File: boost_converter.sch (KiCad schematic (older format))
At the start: 20 parts, among them SW1 SW_Push, U1 LTC2955-1(DFN), U2 LTC3458

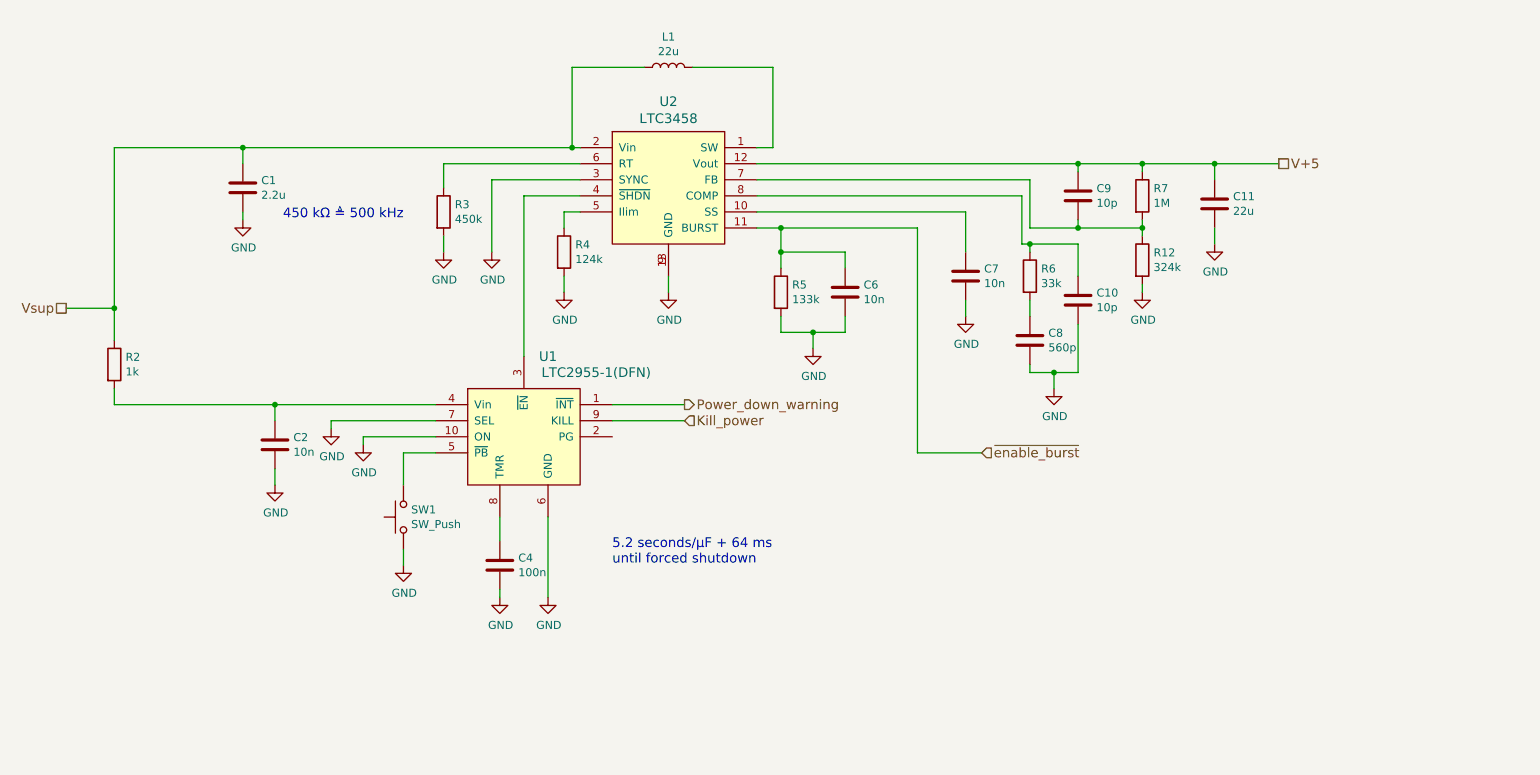
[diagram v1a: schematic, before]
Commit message: Moved MCU pins around to make sure that they do not interfere with the programmer Moved ISP Header closer to the edge of the board to allow easier access with the programmer Added pulldown resistor to the DCD/DC converters enable pin to make sure it stays off in case of failure Added more PDFs of components
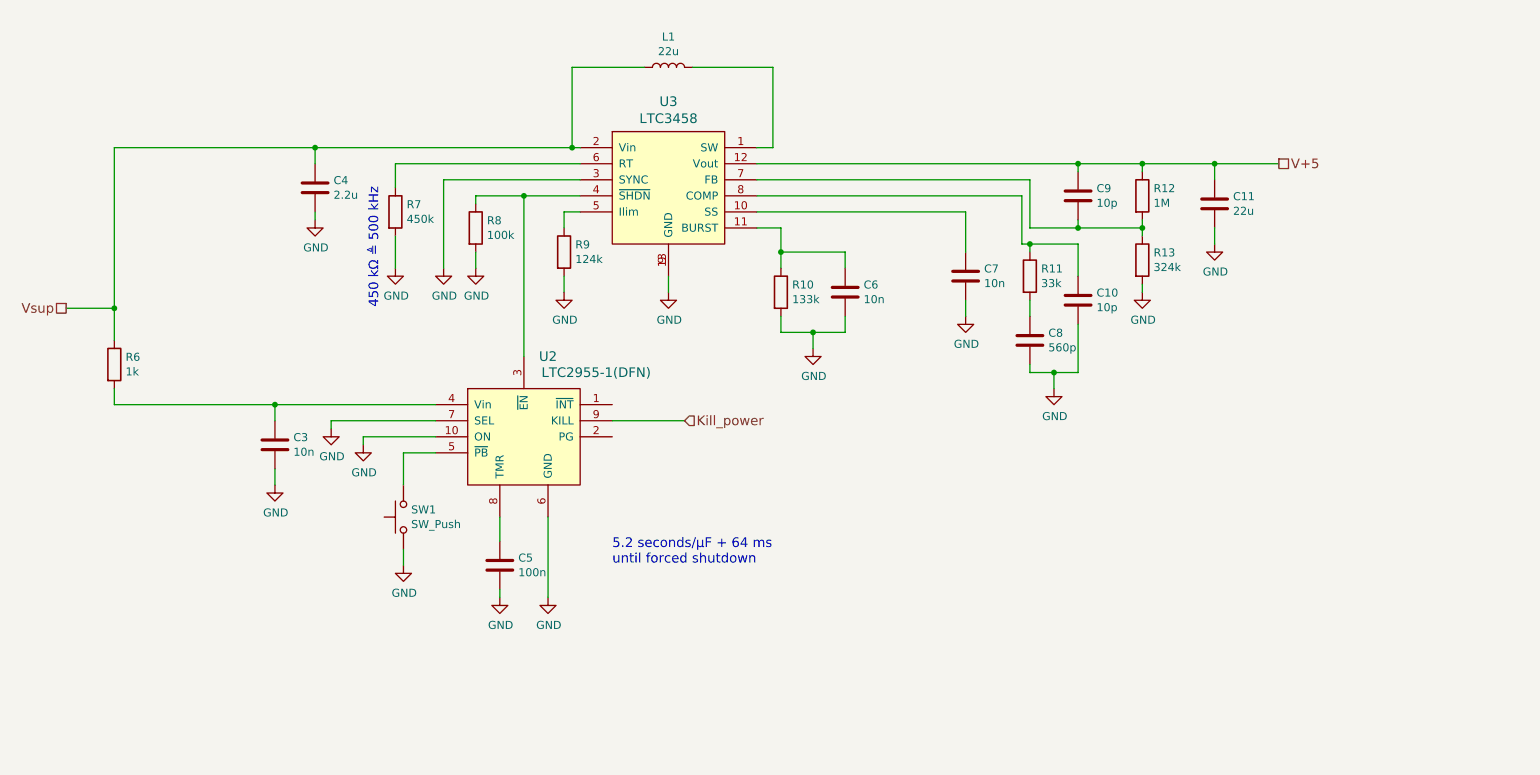
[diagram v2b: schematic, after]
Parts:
- added R8: 100k, Resistors_SMD:R_0603, symbol R
- renumbered C2 to C3, C1 to C4, C4 to C5, R5 to R10, R6 to R11, R7 to R12, R12 to R13, R2 to R6, R3 to R7, R4 to R9, U1 to U2, U2 to U3
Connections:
- net GND: now also R8.2
- net at U2.3 (~EN), U3.4 (~SHDN): now also R8.1
- net Power_down_warning: no longer names the net of U2.1 (~INT)
- net ~enable_burst: no longer names the net of C6.1, R10.1, U3.11 (BURST)
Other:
- moved on the sheet: C4, R7
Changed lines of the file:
@@
 $EndDescr
 $Comp
-L LTC2955-1(DFN) U1
+L LTC2955-1(DFN) U2
 U 1 1 59D06F4F
 P 4850 3600
-F 0 "U1" H 5000 4250 60  0000 C CNN
+F 0 "U2" H 5000 4250 60  0000 C CNN
 F 1 "LTC2955-1(DFN)" H 5300 4150 60  0000 C CNN
 F 2 "Housings_DFN_QFN:DFN-10-1EP_2x3mm_Pitch0.5mm" H 6200 4250 60  0001 C CNN
@@
 Vsup
 $Comp
-L C C2
+L C C3
 U 1 1 59D07029
 P 3300 3500
-F 0 "C2" H 3415 3546 50  0000 L CNN
+F 0 "C3" H 3415 3546 50  0000 L CNN
 F 1 "10n" H 3415 3455 50  0000 L CNN
 F 2 "Capacitors_SMD:C_0603" H 3338 3350 50  0001 C CNN
@@
 $EndComp
 $Comp
-L C C4
+L C C5
 U 1 1 59D073A5
 P 4700 4250
-F 0 "C4" H 4815 4296 50  0000 L CNN
+F 0 "C5" H 4815 4296 50  0000 L CNN
 F 1 "100n" H 4815 4205 50  0000 L CNN
 F 2 "Capacitors_SMD:C_0603" H 4738 4100 50  0001 C CNN
@@
 $EndComp
 $Comp
-L R R2
+L R R6
 U 1 1 59D07A41
 P 2300 3000
-F 0 "R2" H 2370 3046 50  0000 L CNN
+F 0 "R6" H 2370 3046 50  0000 L CNN
 F 1 "1k" H 2370 2955 50  0000 L CNN
 F 2 "Resistors_SMD:R_0603" V 2230 3000 50  0001 C CNN
@@
 $EndComp
 $Comp
-L LTC3458 U2
+L LTC3458 U3
 U 1 1 59D08D68
 P 5750 2000
-AR Path="/59D08D68" Ref="U2"  Part="1"
-AR Path="/59B6A868/59D05F37/59D08D68" Ref="U2"  Part="1"
-F 0 "U2" H 5750 2637 60  0000 C CNN
+F 0 "U3" H 5750 2637 60  0000 C CNN
 F 1 "LTC3458" H 5750 2531 60  0000 C CNN
 F 2 "Housings_DFN_QFN:DFN-12-1EP_3x4mm_Pitch0.5mm" H 7100 2650 60  0001 C CNN
@@
 $EndComp
 $Comp
-L R R3
+L R R7
 U 1 1 59D08F18
-P 4350 2050
-F 0 "R3" H 4420 2096 50  0000 L CNN
-F 1 "450k" H 4420 2005 50  0000 L CNN
-F 2 "Resistors_SMD:R_0603" V 4280 2050 50  0001 C CNN
-F 3 "" H 4350 2050 50  0001 C CNN
-	1    4350 2050
+P 4050 2050
+F 0 "R7" H 4120 2096 50  0000 L CNN
+F 1 "450k" H 4120 2005 50  0000 L CNN
+F 2 "Resistors_SMD:R_0603" V 3980 2050 50  0001 C CNN
+F 3 "" H 4050 2050 50  0001 C CNN
+	1    4050 2050
 	1    0    0    -1
 $EndComp
@@
 L GND #PWR017
 U 1 1 59D08FA8
-P 4350 2300
-F 0 "#PWR017" H 4350 2050 50  0001 C CNN
-F 1 "GND" H 4355 2127 50  0000 C CNN
-F 2 "" H 4350 2300 50  0001 C CNN
-F 3 "" H 4350 2300 50  0001 C CNN
-	1    4350 2300
-	1    0    0    -1
-$EndComp
-Text Notes 3350 2100 0    60   ~ 0
+P 4050 2400
+F 0 "#PWR017" H 4050 2150 50  0001 C CNN
+F 1 "GND" H 4055 2227 50  0000 C CNN
+F 2 "" H 4050 2400 50  0001 C CNN
+F 3 "" H 4050 2400 50  0001 C CNN
+	1    4050 2400
+	1    0    0    -1
+$EndComp
+Text Notes 3950 2650 1    60   ~ 0
 450 kΩ ≜ 500 kHz
 $Comp
 L GND #PWR018
 U 1 1 59D09261
-P 4650 2300
-F 0 "#PWR018" H 4650 2050 50  0001 C CNN
-F 1 "GND" H 4655 2127 50  0000 C CNN
-F 2 "" H 4650 2300 50  0001 C CNN
-F 3 "" H 4650 2300 50  0001 C CNN
-	1    4650 2300
-	1    0    0    -1
-$EndComp
-$Comp
-L R R4
+P 4350 2400
+F 0 "#PWR018" H 4350 2150 50  0001 C CNN
+F 1 "GND" H 4355 2227 50  0000 C CNN
+F 2 "" H 4350 2400 50  0001 C CNN
+F 3 "" H 4350 2400 50  0001 C CNN
+	1    4350 2400
+	1    0    0    -1
+$EndComp
+$Comp
+L R R9
 U 1 1 59D092D3
 P 5100 2300
-F 0 "R4" H 5170 2346 50  0000 L CNN
+F 0 "R9" H 5170 2346 50  0000 L CNN
 F 1 "124k" H 5170 2255 50  0000 L CNN
 F 2 "Resistors_SMD:R_0603" V 5030 2300 50  0001 C CNN
@@
 $EndComp
 $Comp
-L R R7
+L R R12
 U 1 1 59D096F1
 P 8700 1950
-F 0 "R7" H 8770 1996 50  0000 L CNN
+F 0 "R12" H 8770 1996 50  0000 L CNN
 F 1 "1M" H 8770 1905 50  0000 L CNN
 F 2 "Resistors_SMD:R_0603" V 8630 1950 50  0001 C CNN
@@
 $EndComp
 $Comp
-L R R12
+L R R13
 U 1 1 59D09733
 P 8700 2350
-F 0 "R12" H 8770 2396 50  0000 L CNN
+F 0 "R13" H 8770 2396 50  0000 L CNN
 F 1 "324k" H 8770 2305 50  0000 L CNN
 F 2 "Resistors_SMD:R_0603" V 8630 2350 50  0001 C CNN
@@
 $EndComp
 $Comp
-L R R6
+L R R11
 U 1 1 59D09D45
 P 8000 2450
-F 0 "R6" H 8070 2496 50  0000 L CNN
+F 0 "R11" H 8070 2496 50  0000 L CNN
 F 1 "33k" H 8070 2405 50  0000 L CNN
 F 2 "Resistors_SMD:R_0603" V 7930 2450 50  0001 C CNN
@@
 $EndComp
 $Comp
-L R R5
+L R R10
 U 1 1 59D0A192
 P 6450 2550
-F 0 "R5" H 6520 2596 50  0000 L CNN
+F 0 "R10" H 6520 2596 50  0000 L CNN
 F 1 "133k" H 6520 2505 50  0000 L CNN
 F 2 "Resistors_SMD:R_0603" V 6380 2550 50  0001 C CNN
@@
 	6450 2150 6450 2400
 Wire Wire Line
-	6300 2150 7300 2150
-Wire Wire Line
 	7600 2600 7600 2700
 Wire Wire Line
@@
 	5100 2550 5100 2450
 Wire Wire Line
-	4650 1850 4650 2300
-Wire Wire Line
-	5200 1850 4650 1850
-Wire Wire Line
-	4350 2300 4350 2200
-Wire Wire Line
-	4350 1750 4350 1900
-Wire Wire Line
-	5200 1750 4350 1750
-Wire Wire Line
-	4850 1950 5200 1950
+	4350 1850 4350 2400
+Wire Wire Line
+	5200 1850 4350 1850
+Wire Wire Line
+	4050 2400 4050 2200
+Wire Wire Line
+	4050 1750 4050 1900
+Wire Wire Line
+	5200 1750 4050 1750
+Wire Wire Line
+	4550 1950 5200 1950
 Wire Wire Line
 	4850 2950 4850 1950
@@
 Connection ~ 5150 1650
 $Comp
-L C C1
+L C C4
 U 1 1 59D0AC39
-P 3100 1900
-F 0 "C1" H 3215 1946 50  0000 L CNN
-F 1 "2.2u" H 3215 1855 50  0000 L CNN
-F 2 "Capacitors_SMD:C_0603" H 3138 1750 50  0001 C CNN
-F 3 "" H 3100 1900 50  0001 C CNN
-	1    3100 1900
+P 3550 1900
+F 0 "C4" H 3665 1946 50  0000 L CNN
+F 1 "2.2u" H 3665 1855 50  0000 L CNN
+F 2 "Capacitors_SMD:C_0603" H 3588 1750 50  0001 C CNN
+F 3 "" H 3550 1900 50  0001 C CNN
+	1    3550 1900
 	1    0    0    -1
 $EndComp
@@
 L GND #PWR025
 U 1 1 59D0AC9B
-P 3100 2100
-F 0 "#PWR025" H 3100 1850 50  0001 C CNN
-F 1 "GND" H 3105 1927 50  0000 C CNN
-F 2 "" H 3100 2100 50  0001 C CNN
-F 3 "" H 3100 2100 50  0001 C CNN
-	1    3100 2100
-	1    0    0    -1
-$EndComp
-Wire Wire Line
-	3100 2100 3100 2050
-Wire Wire Line
-	3100 1750 3100 1650
-Connection ~ 3100 1650
+P 3550 2100
+F 0 "#PWR025" H 3550 1850 50  0001 C CNN
+F 1 "GND" H 3555 1927 50  0000 C CNN
+F 2 "" H 3550 2100 50  0001 C CNN
+F 3 "" H 3550 2100 50  0001 C CNN
+	1    3550 2100
+	1    0    0    -1
+$EndComp
+Wire Wire Line
+	3550 2100 3550 2050
+Wire Wire Line
+	3550 1750 3550 1650
+Connection ~ 3550 1650
 $Comp
 L C C11
@@
 	9150 1850 9150 1750
 Connection ~ 9150 1750
-Text HLabel 5850 3250 2    60   Output ~ 0
-Power_down_warning
-Wire Wire Line
-	5400 3250 5850 3250
 Text HLabel 5850 3350 2    60   Input ~ 0
 Kill_power
 Wire Wire Line
 	5850 3350 5400 3350
-Text HLabel 7700 3550 2    60   Input ~ 0
-~enable_burst
-Wire Wire Line
-	7300 2150 7300 3550
-Wire Wire Line
-	7300 3550 7700 3550
-Connection ~ 6450 2150
+Wire Wire Line
+	6300 2150 6450 2150
+$Comp
+L GND #PWR027
+U 1 1 5A46F400
+P 4550 2400
+F 0 "#PWR027" H 4550 2150 50  0001 C CNN
+F 1 "GND" H 4555 2227 50  0000 C CNN
+F 2 "" H 4550 2400 50  0001 C CNN
+F 3 "" H 4550 2400 50  0001 C CNN
+	1    4550 2400
+	1    0    0    -1
+$EndComp
+Wire Wire Line
+	4550 2000 4550 1950
+Connection ~ 4850 1950
+Wire Wire Line
+	4550 2300 4550 2400
+$Comp
+L R R8
+U 1 1 5A46F9EB
+P 4550 2150
+F 0 "R8" H 4620 2196 50  0000 L CNN
+F 1 "100k" H 4620 2105 50  0000 L CNN
+F 2 "Resistors_SMD:R_0603" H 4620 2059 50  0001 L CNN
+F 3 "" H 4550 2150 50  0000 C CNN
+	1    4550 2150
+	1    0    0    -1
+$EndComp
 $EndSCHEMATC

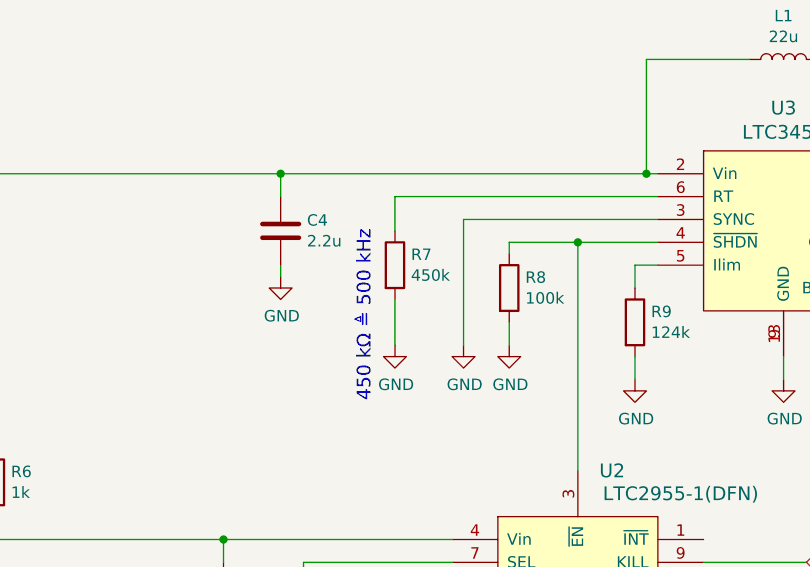
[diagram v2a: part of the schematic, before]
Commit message: Added part names and BOM Added Gerber files
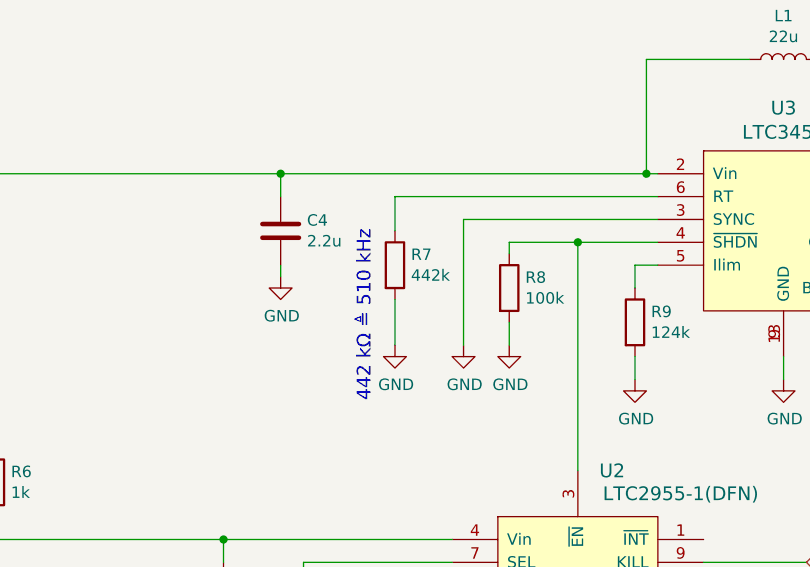
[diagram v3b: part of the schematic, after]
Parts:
- C10, C9: MFN (none) -> Murata; MFP (none) -> GCM1885C1H100FA16D
- C11: MFN (none) -> Murata; MFP (none) -> GRM31CR61E226KE15K
- C3, C6, C7: MFN (none) -> Murata; MFP (none) -> GRM1885C1H103JA01D
- C4: MFN (none) -> Murata; MFP (none) -> GRM188R61E225KA12D
- C5: MFN (none) -> Murata; MFP (none) -> GRM188R71H104KA93D
- C8: MFN (none) -> Murata; MFP (none) -> GCM1885C2A561JA16D
- R10: MFN (none) -> Susumu; MFP (none) -> RR0816P-1333-D-13D
- R11: MFN (none) -> Susumu; MFP (none) -> RR0816P-333-D
- R12: MFN (none) -> Yageo; MFP (none) -> RC0603FR-101ML
- R13: MFN (none) -> Susumu; MFP (none) -> RR0816P-3243-D-50D
- R6: MFN (none) -> Yageo; MFP (none) -> RC0603FR-071KL
- R7: value 450k -> 442k; MFN (none) -> Yageo; MFP (none) -> RT0603DRE07442KL
- R8: MFN (none) -> Yageo; MFP (none) -> RC0603JR-07100KL
- R9: MFN (none) -> Susumu; MFP (none) -> RR0816P-1243-D-10D
- SW1: footprint SW_Tactile_SPST_Angled_PTS645Vx31-2LFS -> Buttons_Switches_THT:SW_Tactile_SPST_Angled_PTS645Vx31-2LFS; MFN (none) -> C&K Components; MFP (none) -> PTS645VL31-2 LFS
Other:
- note added: "442 kΩ ≜ 510 kHz"
- note removed: "450 kΩ ≜ 500 kHz"
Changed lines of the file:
@@
 F 2 "Capacitors_SMD:C_0603" H 3338 3350 50  0001 C CNN
 F 3 "" H 3300 3500 50  0001 C CNN
+F 4 "Murata" H 3300 3500 60  0001 C CNN "MFN"
+F 5 "GRM1885C1H103JA01D" H 3300 3500 60  0001 C CNN "MFP"
 	1    3300 3500
 	1    0    0    -1
@@
 F 0 "SW1" V 4146 3902 50  0000 R CNN
 F 1 "SW_Push" V 4055 3902 50  0000 R CNN
-F 2 "SW_Tactile_SPST_Angled_PTS645Vx31-2LFS" H 4100 4150 50  0001 C CNN
+F 2 "Buttons_Switches_THT:SW_Tactile_SPST_Angled_PTS645Vx31-2LFS" H 4100 4150 50  0001 C CNN
 F 3 "" H 4100 4150 50  0001 C CNN
+F 4 "C&K Components" H 4100 3950 60  0001 C CNN "MFN"
+F 5 "PTS645VL31-2 LFS" H 4100 3950 60  0001 C CNN "MFP"
 	1    4100 3950
 	0    -1   -1   0
@@
 F 2 "Capacitors_SMD:C_0603" H 4738 4100 50  0001 C CNN
 F 3 "" H 4700 4250 50  0001 C CNN
+F 4 "Murata" H 4700 4250 60  0001 C CNN "MFN"
+F 5 "GRM188R71H104KA93D" H 4700 4250 60  0001 C CNN "MFP"
 	1    4700 4250
 	1    0    0    -1
@@
 F 2 "Resistors_SMD:R_0603" V 2230 3000 50  0001 C CNN
 F 3 "" H 2300 3000 50  0001 C CNN
+F 4 "Yageo" H 2300 3000 60  0001 C CNN "MFN"
+F 5 "RC0603FR-071KL" H 2300 3000 60  0001 C CNN "MFP"
 	1    2300 3000
 	1    0    0    -1
@@
 P 4050 2050
 F 0 "R7" H 4120 2096 50  0000 L CNN
-F 1 "450k" H 4120 2005 50  0000 L CNN
+F 1 "442k" H 4120 2005 50  0000 L CNN
 F 2 "Resistors_SMD:R_0603" V 3980 2050 50  0001 C CNN
 F 3 "" H 4050 2050 50  0001 C CNN
+F 4 "Yageo" H 4050 2050 60  0001 C CNN "MFN"
+F 5 "RT0603DRE07442KL" H 4050 2050 60  0001 C CNN "MFP"
 	1    4050 2050
 	1    0    0    -1
@@
 $EndComp
 Text Notes 3950 2650 1    60   ~ 0
-450 kΩ ≜ 500 kHz
+442 kΩ ≜ 510 kHz
 $Comp
 L GND #PWR018
@@
 F 2 "Resistors_SMD:R_0603" V 5030 2300 50  0001 C CNN
 F 3 "" H 5100 2300 50  0001 C CNN
+F 4 "Susumu" H 5100 2300 60  0001 C CNN "MFN"
+F 5 "RR0816P-1243-D-10D" H 5100 2300 60  0001 C CNN "MFP"
 	1    5100 2300
 	1    0    0    -1
@@
 F 2 "Capacitors_SMD:C_0603" H 8338 1800 50  0001 C CNN
 F 3 "" H 8300 1950 50  0001 C CNN
+F 4 "Murata" H 8300 1950 60  0001 C CNN "MFN"
+F 5 "GCM1885C1H100FA16D" H 8300 1950 60  0001 C CNN "MFP"
 	1    8300 1950
 	1    0    0    -1
@@
 F 2 "Resistors_SMD:R_0603" V 8630 1950 50  0001 C CNN
 F 3 "" H 8700 1950 50  0001 C CNN
+F 4 "Yageo" H 8700 1950 60  0001 C CNN "MFN"
+F 5 "RC0603FR-101ML" H 8700 1950 60  0001 C CNN "MFP"
 	1    8700 1950
 	1    0    0    -1
@@
 F 2 "Resistors_SMD:R_0603" V 8630 2350 50  0001 C CNN
 F 3 "" H 8700 2350 50  0001 C CNN
+F 4 "Susumu" H 8700 2350 60  0001 C CNN "MFN"
+F 5 "RR0816P-3243-D-50D" H 8700 2350 60  0001 C CNN "MFP"
 	1    8700 2350
 	1    0    0    -1
@@
 F 2 "Capacitors_SMD:C_0603" H 8038 2700 50  0001 C CNN
 F 3 "" H 8000 2850 50  0001 C CNN
+F 4 "Murata" H 8000 2850 60  0001 C CNN "MFN"
+F 5 "GCM1885C2A561JA16D" H 8000 2850 60  0001 C CNN "MFP"
 	1    8000 2850
 	1    0    0    -1
@@
 F 2 "Capacitors_SMD:C_0603" H 8338 2450 50  0001 C CNN
 F 3 "" H 8300 2600 50  0001 C CNN
+F 4 "Murata" H 8300 2600 60  0001 C CNN "MFN"
+F 5 "GCM1885C1H100FA16D" H 8300 2600 60  0001 C CNN "MFP"
 	1    8300 2600
 	1    0    0    -1
@@
 F 2 "Resistors_SMD:R_0603" V 7930 2450 50  0001 C CNN
 F 3 "" H 8000 2450 50  0001 C CNN
+F 4 "Susumu" H 8000 2450 60  0001 C CNN "MFN"
+F 5 "RR0816P-333-D" H 8000 2450 60  0001 C CNN "MFP"
 	1    8000 2450
 	1    0    0    -1
@@
 F 2 "Capacitors_SMD:C_0603" H 7638 2300 50  0001 C CNN
 F 3 "" H 7600 2450 50  0001 C CNN
+F 4 "Murata" H 7600 2450 60  0001 C CNN "MFN"
+F 5 "GRM1885C1H103JA01D" H 7600 2450 60  0001 C CNN "MFP"
 	1    7600 2450
 	1    0    0    -1
@@
 F 2 "Resistors_SMD:R_0603" V 6380 2550 50  0001 C CNN
 F 3 "" H 6450 2550 50  0001 C CNN
+F 4 "Susumu" H 6450 2550 60  0001 C CNN "MFN"
+F 5 "RR0816P-1333-D-13D" H 6450 2550 60  0001 C CNN "MFP"
 	1    6450 2550
 	1    0    0    -1
@@
 F 2 "Capacitors_SMD:C_0603" H 6888 2400 50  0001 C CNN
 F 3 "" H 6850 2550 50  0001 C CNN
+F 4 "Murata" H 6850 2550 60  0001 C CNN "MFN"
+F 5 "GRM1885C1H103JA01D" H 6850 2550 60  0001 C CNN "MFP"
 	1    6850 2550
 	1    0    0    -1
@@
 F 2 "Capacitors_SMD:C_0603" H 3588 1750 50  0001 C CNN
 F 3 "" H 3550 1900 50  0001 C CNN
+F 4 "Murata" H 3550 1900 60  0001 C CNN "MFN"
+F 5 "GRM188R61E225KA12D" H 3550 1900 60  0001 C CNN "MFP"
 	1    3550 1900
 	1    0    0    -1
@@
 F 2 "Capacitors_SMD:C_1206" H 9188 1850 50  0001 C CNN
 F 3 "" H 9150 2000 50  0001 C CNN
+F 4 "Murata" H 9150 2000 60  0001 C CNN "MFN"
+F 5 "GRM31CR61E226KE15K" H 9150 2000 60  0001 C CNN "MFP"
 	1    9150 2000
 	1    0    0    -1
@@
 F 2 "Resistors_SMD:R_0603" H 4620 2059 50  0001 L CNN
 F 3 "" H 4550 2150 50  0000 C CNN
+F 4 "Yageo" H 4550 2150 60  0001 C CNN "MFN"
+F 5 "RC0603JR-07100KL" H 4550 2150 60  0001 C CNN "MFP"
 	1    4550 2150
 	1    0    0    -1

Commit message: Preparing for v1.2 Updated to KiCAD 5 nightly Added resistors to isolate the programming pins Added transistor to drive the LED Replaced LTC3458 boost converter with an LTC3536 buck-boost converter to step down the USB power supply Added debugging jumper to test the voltage regulator
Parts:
- removed C10, C9: 10p, Capacitors_SMD:C_0603, symbol C
- removed C8: 560p, Capacitors_SMD:C_0603, symbol C
- removed R13: 324k, Resistors_SMD:R_0603, symbol R
- removed R9: 124k, Resistors_SMD:R_0603, symbol R
- removed U3: LTC3458, Housings_DFN_QFN:DFN-12-1EP_3x4mm_Pitch0.5mm, symbol LTC3458
- added C9: 47u, Capacitors_SMD:C_0805, symbol device:C
- added J4, J5: GS2, Custom_footprints:jumper_solder_small, symbol conn:GS2
- added J8: Conn_01x01, Measurement_Points:Measurement_Point_Round-SMD-Pad_Small, symbol conn:Conn_01x01
- added R9: 33k, Resistors_SMD:R_0603, symbol device:R
- added U3: LTC3536, Housings_DFN_QFN:DFN-10-1EP_3x3mm_Pitch0.5mm, symbol Linear-Technology:LTC3536
- C3, C5: symbol C -> device:C
- C4: value 2.2u -> 47u; footprint Capacitors_SMD:C_0603 -> Capacitors_SMD:C_0805; symbol C -> device:C; MFP GRM188R61E225KA12D -> GRM21BR61A476ME15L
- C6: value 10n -> 200p; symbol C -> device:C; MFN Murata -> Kemet; MFP GRM1885C1H103JA01D -> C0603C201K5GACTU
- C7: value 10n -> 18p; symbol C -> device:C; MFN Murata -> Kemet; MFP GRM1885C1H103JA01D -> C0603C180J5GACTU
- C8: renamed from C11; value 22u -> 47u; footprint Capacitors_SMD:C_1206 -> Capacitors_SMD:C_0805; symbol C -> device:C; MFP GRM31CR61E226KE15K -> GRM21BR61A476ME15L
- L1: symbol L -> device:L
- R10: value 133k -> 150k; symbol R -> device:R; MFP RR0816P-1333-D-13D -> RR0816P-154-D
- R11: value 33k -> 22.6k; symbol R -> device:R; MFP RR0816P-333-D -> RR0816P-2262-D-35C
- R12: value 1M -> 1.1M; symbol R -> device:R; MFP RC0603FR-101ML -> RC0603FR-071M1L
- R6: symbol R -> device:R
- R7: renamed from R8; symbol R -> device:R
- R8: renamed from R7; value 442k -> 332k; symbol R -> device:R; MFP RT0603DRE07442KL -> RC0603FR-07332KL
- SW1: symbol SW_Push -> switches:SW_Push
- U2: symbol LTC2955-1(DFN) -> Linear-Technology:LTC2955-1(DFN)
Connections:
- net labels added: ~Kill_power
- net labels removed: Kill_power
- wire segments 70 -> 82
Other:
- note added: "332 kΩ ≜ 300 kHz"
- note added: "Optional:\nClose J4 for debugging\nto always enable the DC/DC\nconverter"
- note added: "Optional:\nClose J5 for debugging\nto keep the DC/DC converter enabled"
- note removed: "442 kΩ ≜ 510 kHz"
- moved on the sheet: C3, C4, C5, C6, C7, C8, R10, R11, R12, R6, R7, R8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
